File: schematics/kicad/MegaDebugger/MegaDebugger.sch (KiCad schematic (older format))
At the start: 2 parts

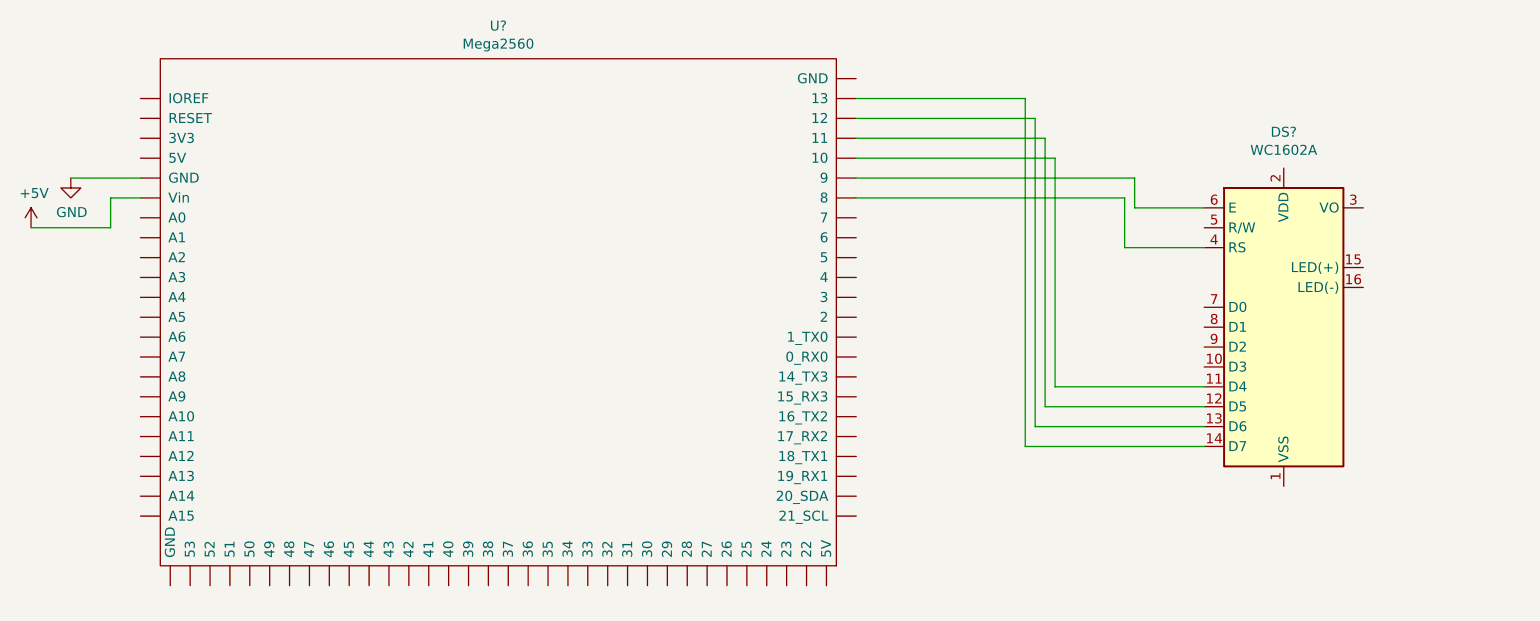
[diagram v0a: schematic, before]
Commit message: Improvements to mega debugger. Working again.
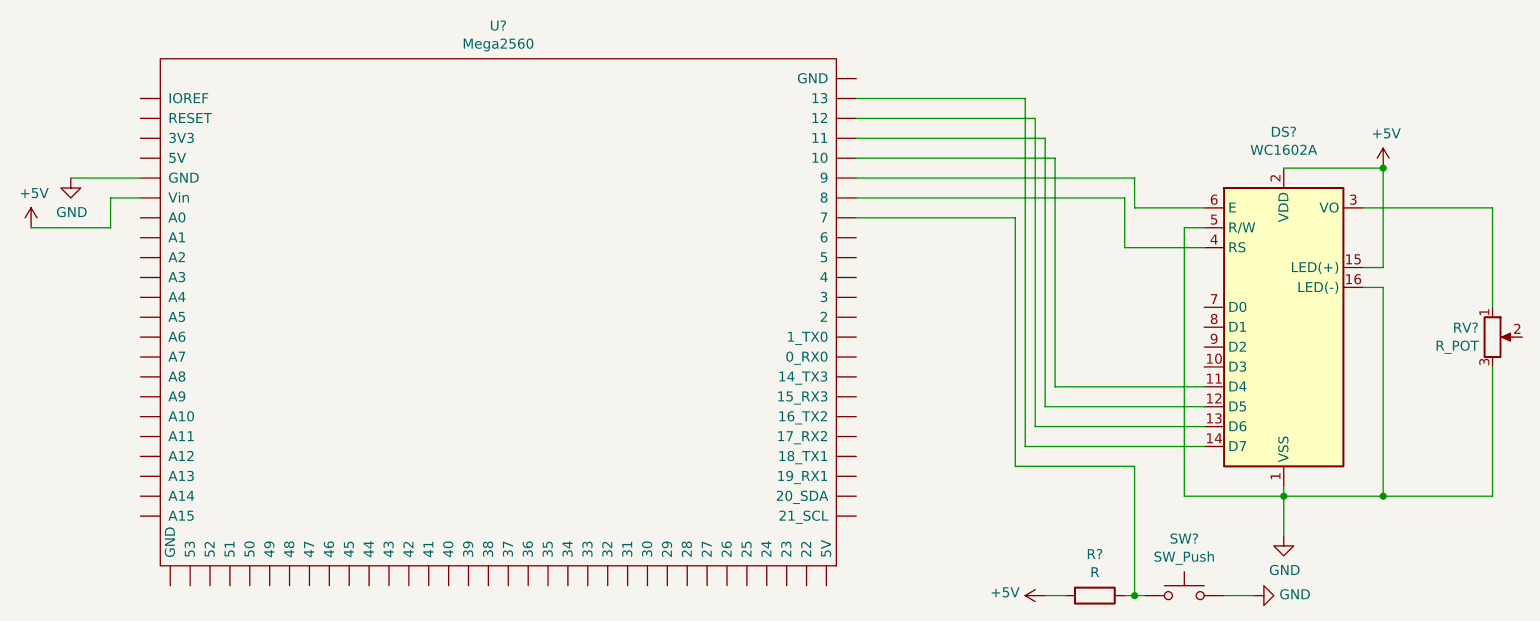
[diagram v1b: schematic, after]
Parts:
- added R?: R, symbol Device:R
- added RV?: R_POT, symbol Device:R_POT
- added SW?: SW_Push, symbol Switch:SW_Push
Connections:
- net +5V: now also DS?.15 (LED(+)), DS?.2 (VDD), R?.2
- net GND: now also DS?.1 (VSS), DS?.16 (LED(-)), DS?.5 (R/W), RV?.3, SW?.2
- net at DS?.3 (VO): now also RV?.1
- new net: R?.1, SW?.1, U?.~ (Vin)
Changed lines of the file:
@@
 EESchema Schematic File Version 4
+LIBS:MegaDebugger-cache
 EELAYER 30 0
 EELAYER END
@@
 Wire Wire Line
 	6600 2150 6600 2400
+$Comp
+L power:GND #PWR?
+U 1 1 60851943
+P 7400 3850
+F 0 "#PWR?" H 7400 3600 50  0001 C CNN
+F 1 "GND" H 7405 3677 50  0000 C CNN
+F 2 "" H 7400 3850 50  0001 C CNN
+F 3 "" H 7400 3850 50  0001 C CNN
+	1    7400 3850
+	1    0    0    -1
+$EndComp
+Wire Wire Line
+	7400 3600 7400 3650
+$Comp
+L power:+5V #PWR?
+U 1 1 6085206B
+P 7900 2000
+F 0 "#PWR?" H 7900 1850 50  0001 C CNN
+F 1 "+5V" H 7915 2173 50  0000 C CNN
+F 2 "" H 7900 2000 50  0001 C CNN
+F 3 "" H 7900 2000 50  0001 C CNN
+	1    7900 2000
+	1    0    0    -1
+$EndComp
+Wire Wire Line
+	7900 2000 7400 2000
+Wire Wire Line
+	7800 2500 7900 2500
+Wire Wire Line
+	7900 2500 7900 2000
+Connection ~ 7900 2000
+Wire Wire Line
+	7800 2600 7900 2600
+Wire Wire Line
+	7900 2600 7900 3650
+Wire Wire Line
+	7900 3650 7400 3650
+Connection ~ 7400 3650
+Wire Wire Line
+	7400 3650 7400 3850
+Wire Wire Line
+	7000 2300 6900 2300
+Wire Wire Line
+	6900 2300 6900 3650
+Wire Wire Line
+	6900 3650 7400 3650
+$Comp
+L Device:R_POT RV?
+U 1 1 60853718
+P 8450 2850
+F 0 "RV?" H 8381 2896 50  0000 R CNN
+F 1 "R_POT" H 8381 2805 50  0000 R CNN
+F 2 "" H 8450 2850 50  0001 C CNN
+F 3 "~" H 8450 2850 50  0001 C CNN
+	1    8450 2850
+	1    0    0    -1
+$EndComp
+Wire Wire Line
+	7800 2200 8450 2200
+Wire Wire Line
+	8450 2200 8450 2700
+Wire Wire Line
+	8450 3000 8450 3650
+Wire Wire Line
+	8450 3650 7900 3650
+Connection ~ 7900 3650
+$Comp
+L power:+5V #PWR?
+U 1 1 60854B43
+P 6200 4150
+F 0 "#PWR?" H 6200 4000 50  0001 C CNN
+F 1 "+5V" V 6215 4278 50  0000 L CNN
+F 2 "" H 6200 4150 50  0001 C CNN
+F 3 "" H 6200 4150 50  0001 C CNN
+	1    6200 4150
+	0    -1   -1   0
+$EndComp
+$Comp
+L Device:R R?
+U 1 1 60855338
+P 6450 4150
+F 0 "R?" V 6243 4150 50  0000 C CNN
+F 1 "R" V 6334 4150 50  0000 C CNN
+F 2 "" V 6380 4150 50  0001 C CNN
+F 3 "~" H 6450 4150 50  0001 C CNN
+	1    6450 4150
+	0    1    1    0
+$EndComp
+$Comp
+L Switch:SW_Push SW?
+U 1 1 60855A2D
+P 6900 4150
+F 0 "SW?" H 6900 4435 50  0000 C CNN
+F 1 "SW_Push" H 6900 4344 50  0000 C CNN
+F 2 "" H 6900 4350 50  0001 C CNN
+F 3 "~" H 6900 4350 50  0001 C CNN
+	1    6900 4150
+	1    0    0    -1
+$EndComp
+$Comp
+L power:GND #PWR?
+U 1 1 60857177
+P 7250 4150
+F 0 "#PWR?" H 7250 3900 50  0001 C CNN
+F 1 "GND" V 7255 4022 50  0000 R CNN
+F 2 "" H 7250 4150 50  0001 C CNN
+F 3 "" H 7250 4150 50  0001 C CNN
+	1    7250 4150
+	0    -1   -1   0
+$EndComp
+Wire Wire Line
+	6300 4150 6200 4150
+Wire Wire Line
+	6600 4150 6650 4150
+Wire Wire Line
+	7100 4150 7250 4150
+Wire Wire Line
+	6650 4150 6650 3500
+Wire Wire Line
+	6650 3500 6050 3500
+Wire Wire Line
+	6050 3500 6050 2250
+Wire Wire Line
+	6050 2250 5250 2250
+Connection ~ 6650 4150
+Wire Wire Line
+	6650 4150 6700 4150
 $EndSCHEMATC
